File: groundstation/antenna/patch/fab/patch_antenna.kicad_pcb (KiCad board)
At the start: 2 copper layers, 160 x 160 mm, 0 parts

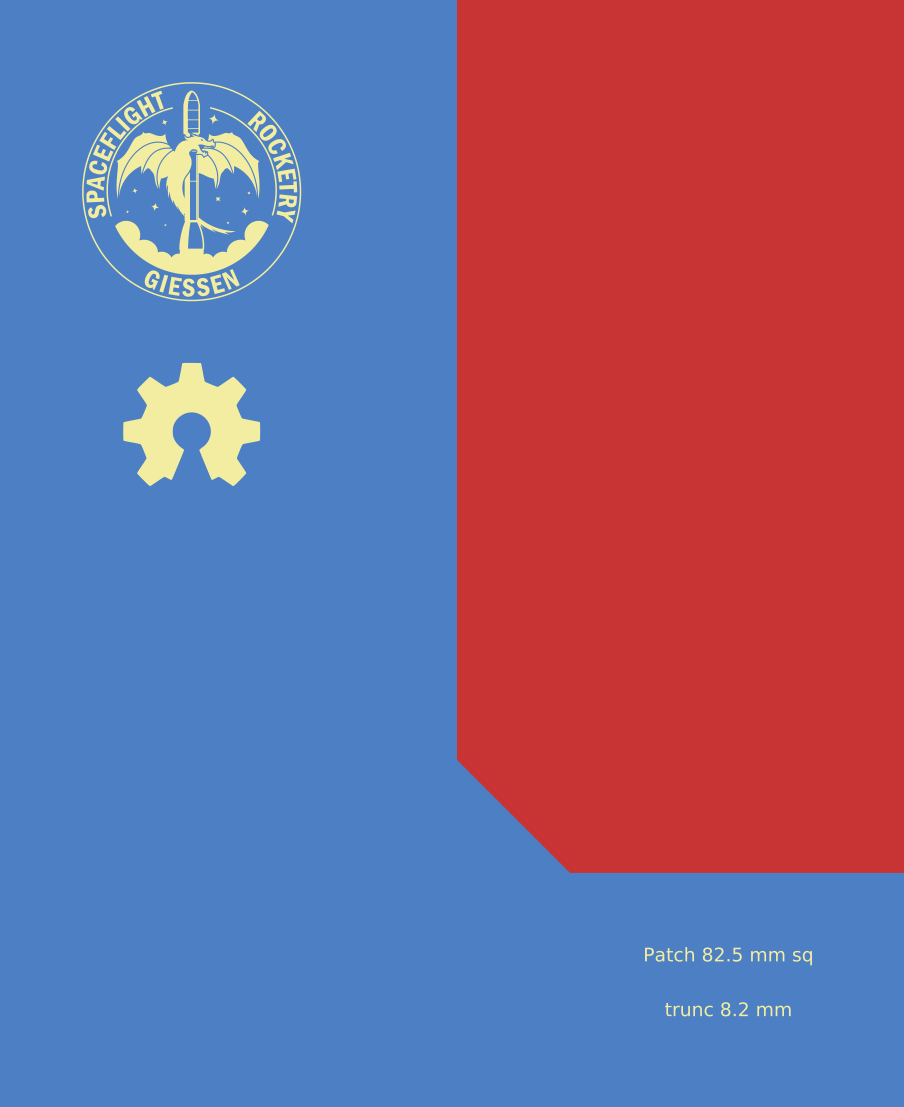
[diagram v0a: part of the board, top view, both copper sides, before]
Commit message: Patch antenna: fix trunc silk label + single-source-of-truth config
Silk: front now reads 'trunc 8.25 mm' (was 8.2 — a .1f rounding bug). Regenerate the board as a KiCad-9 file (restores the back datasheet table + deco disc that a KiCad-10 edit had dropped), re-plot gerbers, refresh the upload zip. SoT: config.py freezes the locked geometry, removing the 82.4937-vs-82.5 split; run.py, enclosure.py and kicad_export.py read dims/mounting/connector MPN from config; kicad_export refuses to build a board whose results.json disagrees with config; add tests/test_no_drift.py (config <-> results.json <-> datasheet). Board and gerbers verified byte-identical (output-neutral); enclosure aligned to 82.5.
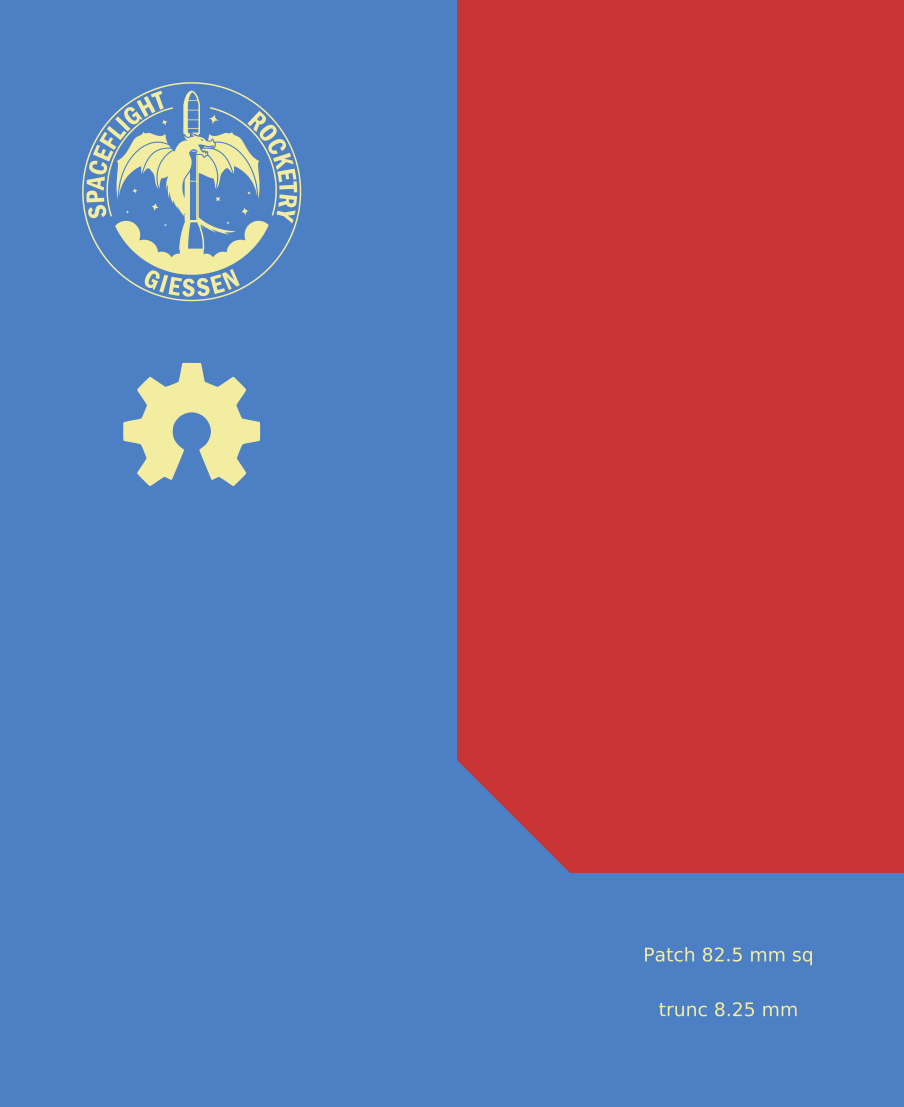
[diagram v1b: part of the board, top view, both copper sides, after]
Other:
- board text added: "trunc 8.25 mm"
- board text removed: "trunc 8.2 mm"
